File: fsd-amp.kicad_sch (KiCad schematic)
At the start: 0 parts

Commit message: add schematic
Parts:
- added C1001, C1003: C_Polarized, symbol Device:C_Polarized
- added C1002: C, symbol Device:C
- added D1001, D1002: D, symbol Device:D
- added J1001: Screw_Terminal_01x06, symbol Connector:Screw_Terminal_01x06
- added J1004: AudioJack2_Ground_Switch, symbol Connector_Audio:AudioJack2_Ground_Switch
- added Q1001, Q1002: Q_NPN_BCE, symbol Device:Q_NPN_BCE
- added Q1003: Q_PNP_BCE, symbol Device:Q_PNP_BCE
- added R1001, R1002: R, symbol Device:R
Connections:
- new net: D1002.1 (K), Q1001.2 (C), Q1003.1 (B), R1001.1
- new net: C1003.1, Q1002.3 (E), Q1003.2 (C)
- new net: D1001.2 (A), Q1002.1 (B), R1002.2
- new net: C1002.2, Q1001.1 (B), R1001.2
- new net: D1001.1 (K), D1002.2 (A)
- new net +9V: C1001.1, J1001.5 (Pin_5), Q1002.2 (C), R1002.1
- new net GND: C1001.2, J1001.2 (Pin_2), J1001.4 (Pin_4), J1001.6 (Pin_6), J1004.G, Q1001.3 (E), Q1003.3 (E)
- new net amp_in: C1002.1, J1001.1 (Pin_1), J1004.S, J1004.SN, J1004.T, J1004.TN
- new net amp_out: C1003.2, J1001.3 (Pin_3)

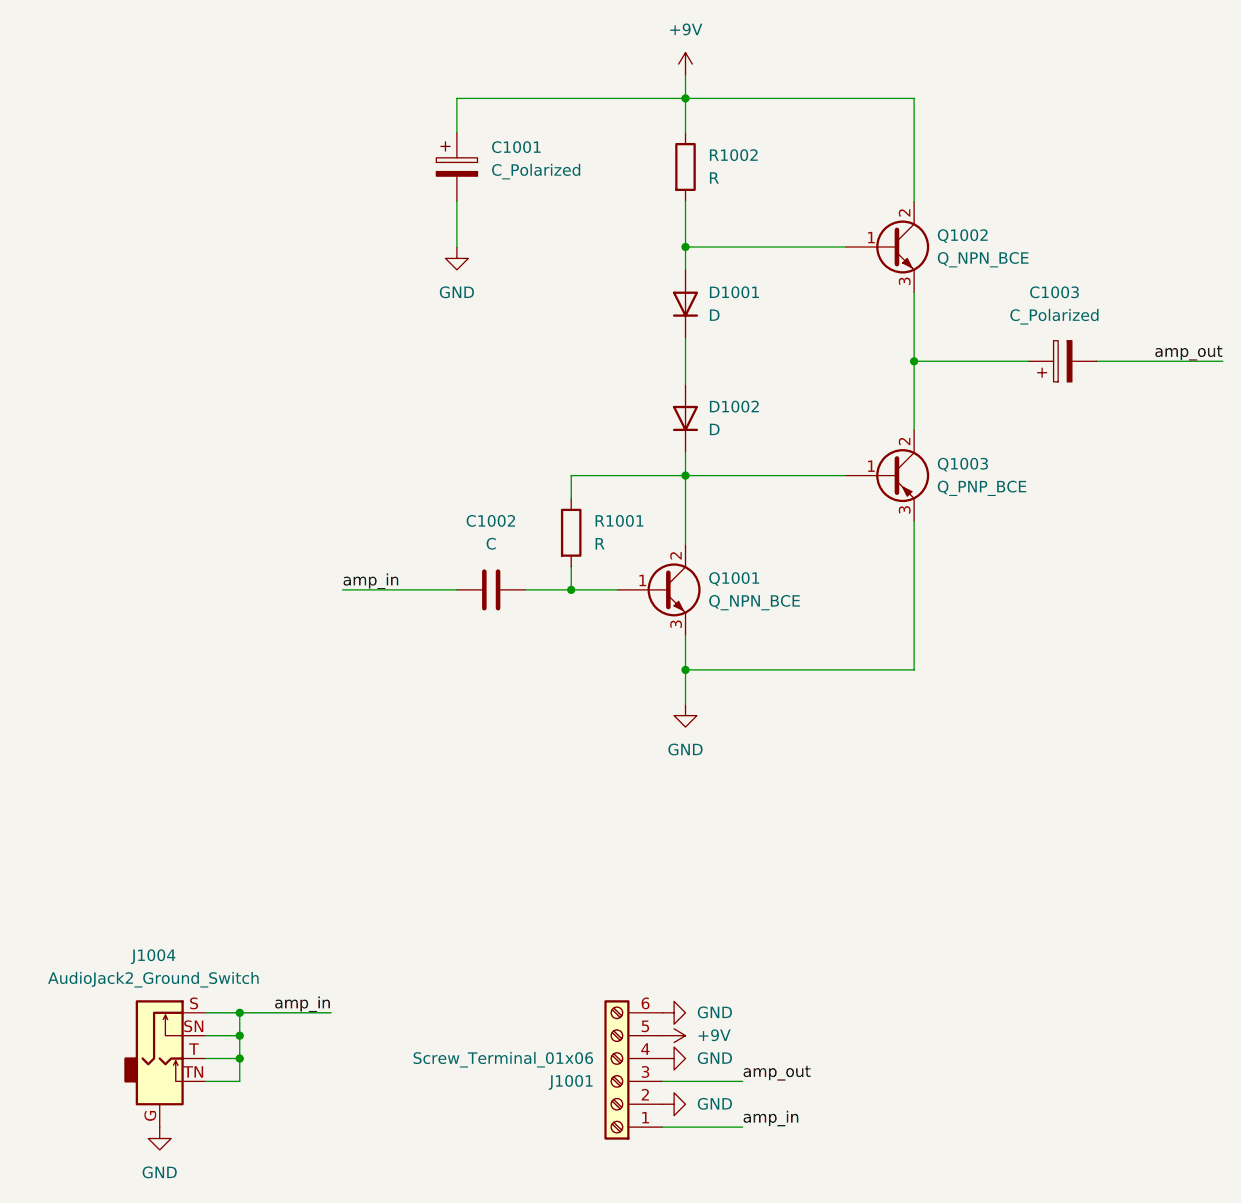
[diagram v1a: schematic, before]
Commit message: add parts from reichelt
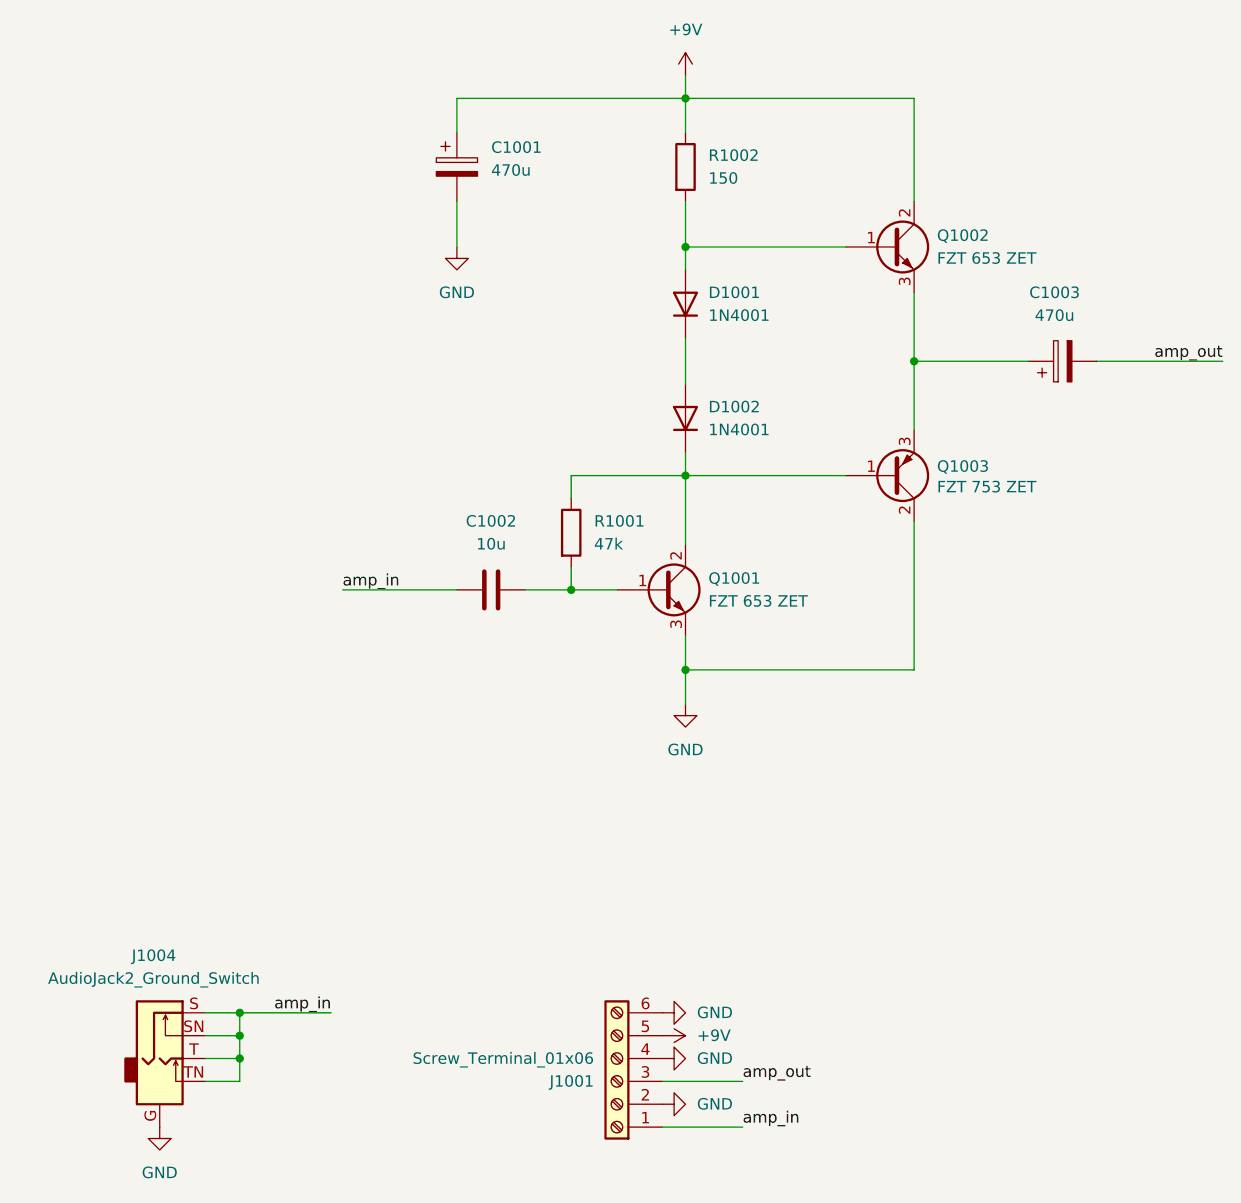
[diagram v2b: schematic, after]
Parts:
- C1001, C1003: value C_Polarized -> 470u; VLNK (none) -> https://www.reichelt.de/elko-radial-470-f-16-v-rm-5-0-85-c-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; VPN (none) -> RAD 470/16
- C1002: value C -> 10u; VLNK (none) -> https://www.reichelt.de/mks2-pet-kondensator-10-f-5-50-vdc-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; VPN (none) -> MKS2-50 10µ
- D1001, D1002: value D -> 1N4001; VLNK (none) -> https://www.reichelt.de/gleichrichterdiode-50-v-1-a-do-41-1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; VPN (none) -> 1N 4001
- J1001: VLNK (none) -> https://www.reichelt.de/anschlussklemme-6-pol-2-mm-rm-5-08-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; VPN (none) -> AKL 101-06
- J1004: VLNK (none) -> https://www.reichelt.de/klinkeneinbaubuchse-3-5-mm-stereo-e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; VPN (none) -> EBS 35
- Q1001, Q1002: value Q_NPN_BCE -> FZT 653 ZET; VLNK (none) -> https://www.reichelt.de/bipolartransistor-npn-100-v-2-a-2-w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; VPN (none) -> FZT 653 ZET
- Q1003: value Q_PNP_BCE -> FZT 753 ZET; VLNK (none) -> https://www.reichelt.de/bipolartransistor-pnp-100-v-2-a-2-w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; VPN (none) -> FZT 753 ZET
- R1001: value R -> 47k; VLNK (none) -> https://www.reichelt.de/widerstand-metallschicht-47-0-kohm-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; VPN (none) -> METALL 47,0K
- R1002: value R -> 150; VLNK (none) -> https://www.reichelt.de/widerstand-metallschicht-150-ohm-02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; VPN (none) -> METALL 150
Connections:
- net GND: now also Q1003.2 (C); no longer Q1003.3 (E)
- net at C1003.1, Q1002.3 (E): now also Q1003.3 (E); no longer Q1003.2 (C)

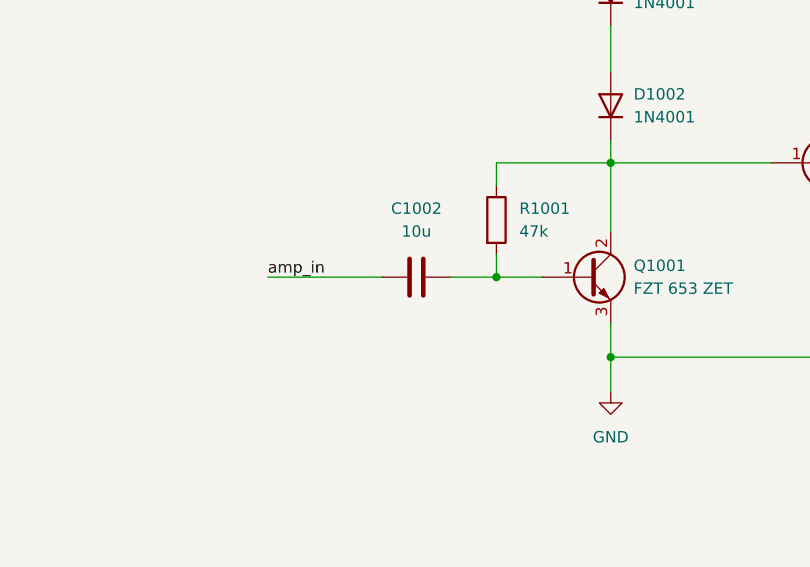
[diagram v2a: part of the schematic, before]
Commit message: add poti for volume adjustment
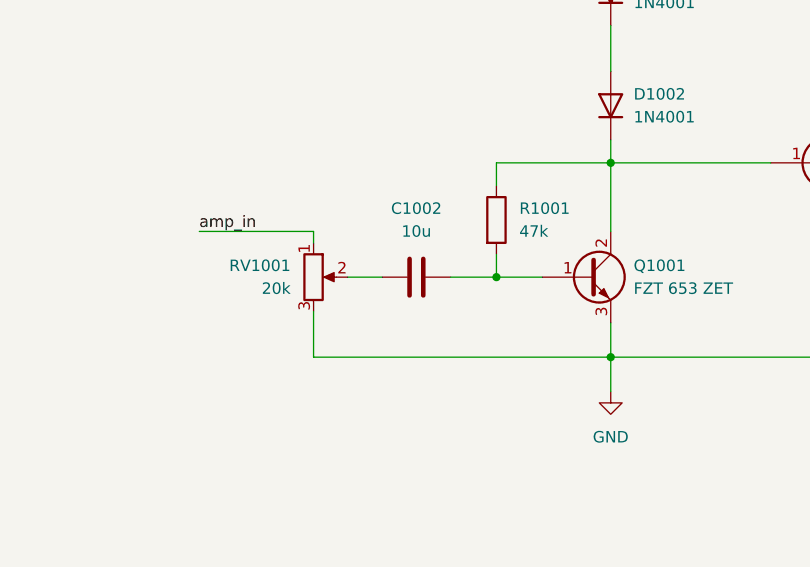
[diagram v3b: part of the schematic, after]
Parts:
- added RV1001: 20k, symbol Device:R_Potentiometer
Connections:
- net GND: now also RV1001.3
- net amp_in: now also RV1001.1; no longer C1002.1
- new net: C1002.1, RV1001.2
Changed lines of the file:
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@@
+	(wire
+		(pts
+			(xy 118.11 119.38) (xy 121.92 119.38)
+		)
+		(stroke
+			(width 0)
+			(type default)
+		)
+	)
 	(wire
 		(pts
@@
 	(wire
 		(pts
+			(xy 101.6 114.3) (xy 114.3 114.3)
+		)
+		(stroke
+			(width 0)
+			(type default)
+		)
+	)
+	(wire
+		(pts
 			(xy 172.72 86.36) (xy 172.72 93.98)
 		)
@@
 	(wire
 		(pts
+			(xy 114.3 128.27) (xy 147.32 128.27)
+		)
+		(stroke
+			(width 0)
+			(type default)
+		)
+	)
+	(wire
+		(pts
 			(xy 147.32 76.2) (xy 147.32 81.28)
 		)
@@
 	(wire
 		(pts
+			(xy 114.3 123.19) (xy 114.3 128.27)
+		)
+		(stroke
+			(width 0)
+			(type default)
+		)
+	)
+	(wire
+		(pts
 			(xy 93.98 173.99) (xy 97.79 173.99)
 		)
@@
 	(wire
 		(pts
+			(xy 114.3 115.57) (xy 114.3 114.3)
+		)
+		(stroke
+			(width 0)
+			(type default)
+		)
+	)
+	(wire
+		(pts
 			(xy 134.62 119.38) (xy 134.62 116.84)
 		)
@@
 		(pts
 			(xy 121.92 68.58) (xy 121.92 64.77)
-		)
-		(stroke
-			(width 0)
-			(type default)
-		)
-	)
-	(wire
-		(pts
-			(xy 109.22 119.38) (xy 121.92 119.38)
 		)
 		(stroke
@@
 	)
 	(label "amp_in"
-		(at 109.22 119.38 0)
+		(at 101.6 114.3 0)
 		(fields_autoplaced yes)
 		(effects
@@
 					(unit 1)
 				)
+			)
+		)
+	)
+	(symbol
+		(lib_id "Device:R_Potentiometer")
+		(at 114.3 119.38 0)
+		(unit 1)
+		(exclude_from_sim no)
+		(in_bom yes)
+		(on_board yes)
+		(dnp no)
+		(fields_autoplaced yes)
+		(property "Reference" "RV1001"
+			(at 111.76 118.1099 0)
+			(effects
+				(font
+					(size 1.27 1.27)
+				)
+				(justify right)
+			)
+		)
+		(property "Value" "20k"
+			(at 111.76 120.6499 0)
+			(effects
+				(font
+					(size 1.27 1.27)
+				)
+				(justify right)
+			)
+		)
+		(property "Footprint" ""
+			(at 114.3 119.38 0)
+			(effects
+				(font
+					(size 1.27 1.27)
+				)
+				(hide yes)
+			)
+		)
+		(property "Datasheet" "https://cdn-reichelt.de/documents/datenblatt/B300/3386_ENG_TDS.pdf"
+			(at 114.3 119.38 0)
+			(effects
+				(font
+					(size 1.27 1.27)
+				)
+				(hide yes)
+			)
+		)
+		(property "Description" "Potentiometer"
+			(at 114.3 119.38 0)
+			(effects
+				(font
+					(size 1.27 1.27)
+				)
+				(hide yes)
+			)
+		)
+		(property "VLNK" "https://www.reichelt.de/praezisionspotentiometer-trimmer-liegend-20-kohm-9-5-mm-76-10-20k-p3495.html?&trstct=pos_0&nbc=1"
+			(at 114.3 119.38 0)
+			(effects
+				(font
+					(size 1.27 1.27)
+				)
+				(hide yes)
+			)
+		)
+		(property "VPN" "76-10 20K"
+			(at 114.3 119.38 0)
+			(effects
+				(font
+					(size 1.27 1.27)
+				)
+				(hide yes)
+			)
+		)
+		(pin "3"
+		)
+		(pin "1"
+		)
+		(pin "2"
+		)
+		(instances
+			(project "fsd-amp"
+				(path "/c6324701-a04d-49c0-9990-add1f54dd7f2"
+					(reference "RV1001")
+					(unit 1)
+				)

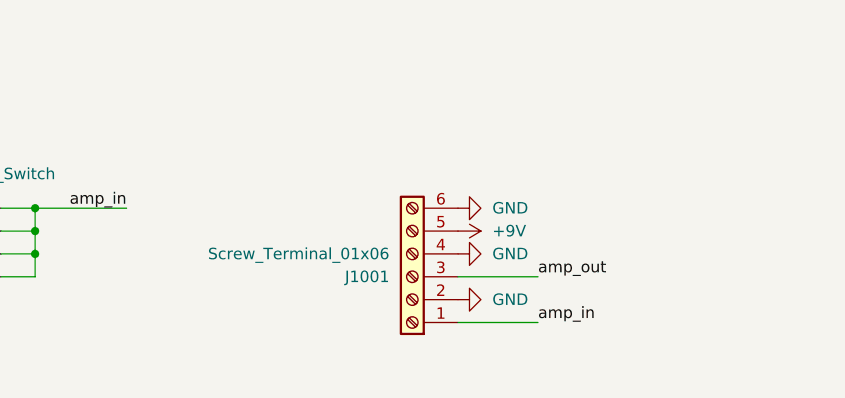
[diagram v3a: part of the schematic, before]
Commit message: fix ERC pwr_flag error
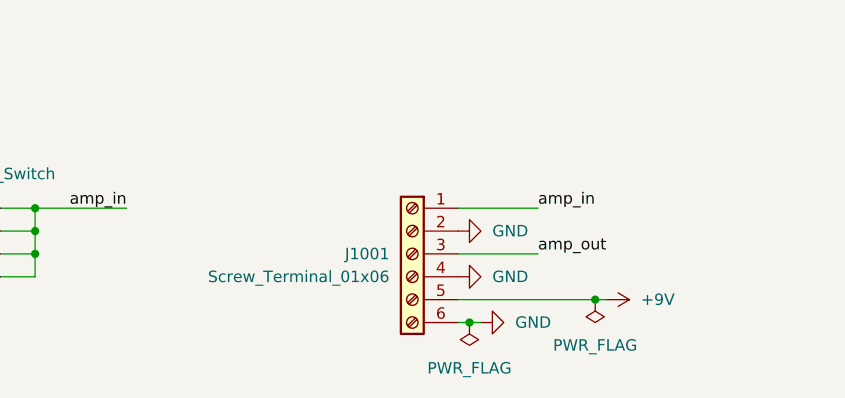
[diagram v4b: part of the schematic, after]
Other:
- moved on the sheet: J1001

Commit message: add footprints
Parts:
- C1001, C1003: footprint (none) -> Capacitor_THT:CP_Radial_D10.0mm_P5.00mm
- C1002: footprint (none) -> Capacitor_THT:C_Rect_L7.2mm_W11.0mm_P5.00mm_FKS2_FKP2_MKS2_MKP2
- D1001, D1002: footprint (none) -> Diode_THT:D_DO-41_SOD81_P10.16mm_Horizontal
- J1001: footprint (none) -> TerminalBlock_MetzConnect:TerminalBlock_MetzConnect_Type101_RT01606HBWC_1x06_P5.08mm_Horizontal
- J1004: footprint (none) -> Connector_Audio:Jack_3.5mm_Ledino_KB3SPRS_Horizontal
- Q1001, Q1002, Q1003: footprint (none) -> Package_TO_SOT_SMD:SOT-223-3_TabPin2
- R1001, R1002: footprint (none) -> Resistor_THT:R_Axial_DIN0207_L6.3mm_D2.5mm_P10.16mm_Horizontal
- RV1001: footprint (none) -> Potentiometer_THT:Potentiometer_Bourns_3296W_Vertical; VLNK https://www.reichelt.de/praezisionspotentiometer-trimmer-li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 -> https://www.reichelt.de/praezisionspotentiometer-25-gaenge-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; VPN 76-10 20K -> 64W-20K
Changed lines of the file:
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@@
 			)
 		)
-		(property "Footprint" ""
+		(property "Footprint" "TerminalBlock_MetzConnect:TerminalBlock_MetzConnect_Type101_RT01606HBWC_1x06_P5.08mm_Horizontal"
 			(at 139.7 171.45 0)
 			(effects
@@
 			)
 		)
-		(property "Footprint" ""
+		(property "Footprint" "Package_TO_SOT_SMD:SOT-223-3_TabPin2"
 			(at 175.26 109.22 0)
 			(effects
@@
 			)
 		)
-		(property "Footprint" ""
+		(property "Footprint" "Potentiometer_THT:Potentiometer_Bourns_3296W_Vertical"
 			(at 114.3 119.38 0)
 			(effects
@@
 			)
 		)
-		(property "Datasheet" "https://cdn-reichelt.de/documents/datenblatt/B300/3386_ENG_TDS.pdf"
+		(property "Datasheet" "https://www.reichelt.de/praezisionspotentiometer-25-gaenge-stehend-20-kohm-64w-20k-p2705.html?&trstct=pol_2&nbc=1"
 			(at 114.3 119.38 0)
 			(effects
@@
 			)
 		)
-		(property "VLNK" "https://www.reichelt.de/praezisionspotentiometer-trimmer-liegend-20-kohm-9-5-mm-76-10-20k-p3495.html?&trstct=pos_0&nbc=1"
+		(property "VLNK" "https://www.reichelt.de/praezisionspotentiometer-25-gaenge-stehend-20-kohm-64w-20k-p2705.html?&trstct=pol_2&nbc=1"
 			(at 114.3 119.38 0)
 			(effects
@@
 			)
 		)
-		(property "VPN" "76-10 20K"
+		(property "VPN" "64W-20K"
 			(at 114.3 119.38 0)
 			(effects
@@
 			)
 		)
-		(property "Footprint" ""
+		(property "Footprint" "Package_TO_SOT_SMD:SOT-223-3_TabPin2"
 			(at 175.26 78.74 0)
 			(effects
@@
 			)
 		)
-		(property "Footprint" ""
+		(property "Footprint" "Resistor_THT:R_Axial_DIN0207_L6.3mm_D2.5mm_P10.16mm_Horizontal"
 			(at 145.542 72.39 90)
 			(effects
@@
 			)
 		)
-		(property "Footprint" ""
+		(property "Footprint" "Capacitor_THT:CP_Radial_D10.0mm_P5.00mm"
 			(at 193.04 93.0148 0)
 			(effects
@@
 			)
 		)
-		(property "Footprint" ""
+		(property "Footprint" "Package_TO_SOT_SMD:SOT-223-3_TabPin2"
 			(at 149.86 116.84 0)
 			(effects
@@
 			)
 		)
-		(property "Footprint" ""
+		(property "Footprint" "Diode_THT:D_DO-41_SOD81_P10.16mm_Horizontal"
 			(at 147.32 87.63 0)
 			(effects
@@
 			)
 		)
-		(property "Footprint" ""
+		(property "Footprint" "Connector_Audio:Jack_3.5mm_Ledino_KB3SPRS_Horizontal"
 			(at 88.9 166.37 0)
 			(effects
@@
 			)
 		)
-		(property "Footprint" ""
+		(property "Footprint" "Resistor_THT:R_Axial_DIN0207_L6.3mm_D2.5mm_P10.16mm_Horizontal"
 			(at 132.842 113.03 90)
 			(effects
@@
 			)
 		)
-		(property "Footprint" ""
+		(property "Footprint" "Capacitor_THT:C_Rect_L7.2mm_W11.0mm_P5.00mm_FKS2_FKP2_MKS2_MKP2"
 			(at 129.54 118.4148 0)
 			(effects
@@
 			)
 		)
-		(property "Footprint" ""
+		(property "Footprint" "Diode_THT:D_DO-41_SOD81_P10.16mm_Horizontal"
 			(at 147.32 100.33 0)
 			(effects
@@
 			)
 		)
-		(property "Footprint" ""
+		(property "Footprint" "Capacitor_THT:CP_Radial_D10.0mm_P5.00mm"
 			(at 122.8852 76.2 0)
 			(effects
